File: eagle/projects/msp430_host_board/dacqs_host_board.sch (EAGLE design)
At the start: 31 parts, among them J1 MOL-KK-4P-V, J2 MOL-KK-4P-V, J3 MOL-KK-4P-V, J4 MOL-KK-4P-V, J5 MOL-KK-5P-V, J6 MOL-KK-3P-V, U1 Value, U2 Value, Y1 32.768kHz, Y2 4MHz, Y3 32.768kHz, Y4 4MHz

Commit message: Changes to MSP connections
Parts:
- added J7: MOL-KK-5P-V, daqcs_host:MOLKK_5PIN_5RA_RA
- added J8: MOL-KK-3P-RA, daqcs_host:MOLKK_3PIN_3RA_RA
- added R4, R5, R6, R7: 2.61k, daqcs_host:RES_2R61_0603
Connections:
- removed net SD_CS: U2.P4.0_A8
- removed net SENSE_SCL: U2.P6.5_UCB3SOMI_UCB3SCL
- removed net SENSE_SDA: U2.P6.4_UCB3SIMO_UCB3SDA
- new net SD_SS: U2.P5.7_UCA2STE_TA4.1_MCLK
- new net SENSE_SCL_1: R4.1, U2.P1.7_TB0.4_UCB0SOMI_UCB0SCL_TA1.0
- new net SENSE_SCL_2: R7.1, U2.P5.1_UCB1SOMI_UCB1SCL
- new net SENSE_SDA_1: R5.1, U2.P1.6_TB0.3_UCB0SIMO_UCB0SDA_TA0.0
- new net SENSE_SDA_2: R6.1, U2.P5.0_UCB1SIMO_UCB1SDA
- net +3V3: now also R4.2, R5.2, R6.2, R7.2
- net ACT_CURRENT_IN: now also J8.2
- net ACT_SPEED_IN: now also J8.1
- net COMMS_MISO: now also U1.P5.1_UCB1SOMI_UCB1SCL; no longer U1.P7.1_UCB2SOMI_UCB2SCL
- net COMMS_MOSI: now also U1.P5.0_UCB1SIMO_UCB1SDA; no longer U1.P7.0_UCB2SIMO_UCB2SDA
- net COMMS_SCLK: now also U1.P5.2_UCB1CLK_TA4CLK; no longer U1.P7.2_UCB2CLK
- net COMMS_SS: now also U1.P5.3_UCB1STE; no longer U1.P1.5_TB0.2_UCA0CLK_A5_C5
- net CURRENT_PWM_OUT: now also J7.2, U2.P1.3_TA1.2_UCB0STE_A3_C3; no longer U2.P3.7_TB0.6
- net DIR_MOTOR_OUT: now also J7.4
- net EN_MOTOR_OUT: now also J7.3
- net GND: now also J7.5, J8.3
- net IMU_MISO: now also U2.P2.6_TB0.1_UCA1RXD_UCA1SOMI; no longer U2.P7.1_UCB2SOMI_UCB2SCL
- net IMU_MOSI: now also U2.P2.5_TB0.0_UCA1TXD_UCA1SIMO; no longer U2.P7.0_UCB2SIMO_UCB2SDA
- net IMU_SCLK: now also U2.P2.4_TA1.0_UCA1CLK_A7_C11; no longer U2.P7.2_UCB2CLK
- net IMU_SS: now also U2.P2.3_TA0.0_UCA1STE_A6_C10; no longer U2.P1.5_TB0.2_UCA0CLK_A5_C5
- net MSP_MISO: now also U1.P1.7_TB0.4_UCB0SOMI_UCB0SCL_TA1.0, U2.P2.1_TB0.0_UCA0RXD_UCA0SOMI; no longer U1.P5.1_UCB1SOMI_UCB1SCL, U2.P5.1_UCB1SOMI_UCB1SCL
- net MSP_MOSI: now also U1.P1.6_TB0.3_UCB0SIMO_UCB0SDA_TA0.0, U2.P2.0_TB0.6_UCA0TXD_UCA0SIMO_TB0CLK_ACLK; no longer U1.P5.0_UCB1SIMO_UCB1SDA, U2.P5.0_UCB1SIMO_UCB1SDA
- net MSP_SCLK: now also U1.P2.2_TB0.2_UCB0CLK, U2.P1.5_TB0.2_UCA0CLK_A5_C5; no longer U1.P5.2_UCB1CLK_TA4CLK, U2.P5.2_UCB1CLK_TA4CLK
- net MSP_SS: now also U1.P1.3_TA1.2_UCB0STE_A3_C3; no longer U1.P1.4_TB0.1_UCA0STE_A4_C4
- net SD_MISO: now also U2.P5.5_UCA2RXD_UCA2SOMI_ACLK; no longer U2.P1.7_TB0.4_UCB0SOMI_UCB0SCL_TA1.0
- net SD_MOSI: now also U2.P5.4_UCA2TXD_UCA2SIMO_TB0OUTH; no longer U2.P1.6_TB0.3_UCB0SIMO_UCB0SDA_TA0.0
- net SD_SCLK: now also U2.P5.6_UCA2CLK_TA4.0_SMCLK; no longer U2.P2.2_TB0.2_UCB0CLK
- net SPEED_PWM_OUT: now also J7.1, U2.P1.2_TA1.1_TA0CLK_COUT_A2_C2; no longer U2.P3.6_TB0.5

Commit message: Added sensors, sd card and updated msp pinout for motor control
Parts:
- added C16: 1000pF, daqcs_host:CAP_1000PF0_0603
- added C17, C18, C20: 100nF, daqcs_host:CAP_100NF0_0603
- added C19: 1uF, daqcs_host:CAP_1UF0_0603
- added J10, J9: MOL-KK-3P-V, daqcs_host:MOLKK_3PIN_3V_V
- added J11: CLM-112-02-L-D, SAMTEC-BCS-CES-CLx_By_element14_Batch_1:CLM-112-02-L-D
- added J12: (no value), SparkFun-Connectors:M02PTH
- added R10, R11, R12, R13, R14, R15, R9: 0, daqcs_host:RES_0R0_0603
- added R16, R8: 47k, daqcs_host:RES_47R0_0603
- added R17: 100k, daqcs_host:RES_100R0_0603
- added S2: SWITCH-MOMENTARY-2PTH, daqcs_host:SWITCH-MOMENTARY-2PTH
- added U$1: MICROSD, daqcs_host:MICROSD
- added U3: PCT2075D,118, daqcs_host:PCT2075D,118SOIC8
- added U4: MS560702BA03-50, daqcs_host:MS5607-02BA03_8SMD
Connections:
- new net +5V: J11.10, J11.11, J11.12
- new net IMU_RST: J12.2, U2.P2.7
- new net N$22: R9.2, U3.A0
- new net N$23: R10.2, U3.A1
- new net N$24: R11.2, U3.A2
- new net N$25: R12.1, U3.OS
- new net N$26: R12.2
- new net N$27: R15.2, U4.CSB@1
- new net N$28: R14.2, U4.CSB@2
- new net N$29: R13.1, U4.SDO
- new net N$30: R13.2
- new net N$32: J11.8, J12.1
- new net N$34: R17.2, U$1.CARD_DETECT1
- new net SD_CS: R16.2, U$1.CS, U2.P4.2_A10
- net +3V3: now also C17.1, C18.1, C19.1, C20.1, R16.1, R17.1, R8.2, U$1.VDD, U3.VCC, U4.PS, U4.VDD
- net ACT_CURRENT_IN: now also U2.P3.1_A13_C13; no longer U2.P3.0_A12_C12
- net ACT_SPEED_IN: now also U2.P3.0_A12_C12; no longer U2.P3.1_A13_C13
- net DIR_MOTOR_OUT: now also U2.P4.1_A9; no longer U2.P4.3_A11
- net EN_MOTOR_OUT: now also U2.P4.0_A8; no longer U2.P4.2_A10
- net GND: now also C16.1, C17.2, C18.2, C19.2, C20.2, J10.3, J11.13, J11.14, J11.15, J9.3, R10.1, R11.1, R14.1, R15.1, R9.1, S2.1, U$1.CARD_DETECT, U$1.GND, U$1.GND1, U$1.VSS, U3.GND, U4.GND
- net IMU_MISO: now also J11.4
- net IMU_MOSI: now also J11.5
- net IMU_SCLK: now also J11.3
- net IMU_SS: now also J11.6
- net RST_SBWTDIO_MOTOR: now also C16.2, J10.1, R8.1, S2.2
- net SBWTCK_MOTOR: now also J10.2
- net SD_DETECT: now also U2.P3.2_A14_C14; no longer U2.P4.5
- net SD_MISO: now also U$1.DATA_OUT
- net SD_MOSI: now also U$1.DATA_IN
- net SD_SCLK: now also U$1.SCLK
- net SENSE_SCL_1: now also U3.SCL, U4.SCLK
- net SENSE_SCL_2: now also J9.2
- net SENSE_SDA_1: now also U3.SDA, U4.SDI/SDA
- net SENSE_SDA_2: now also J9.1
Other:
- note added: "IMU Connector Header"
- note added: "Jumper header to disable RST if necessary"
- note added: "Pressure Sensor"
- note added: "SD Card Connector"
- note added: "Temperature Sensor"

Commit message: Added Power Management schematic
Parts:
- added C21: 2.2uF, daqcs_host:CAP_2UF2_0603
- added C22: 4.7uF, daqcs_host:CAP_4UF7_0603
- added C23, C24: 1uF, daqcs_host:CAP_1UF0_0603
- added J13: MOL-KK-2-V, daqcs_host:MOLKK_2PIN2V_2V
- added U5: TPS61240DRVR, daqcs_host:TPS61240DRVR
- added U6: LP5907_DBV_5, daqcs_host:LP5907_DBV_5
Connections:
- new net N$36: C21.1, J13.1, U5.EN, U5.VIN
- net +3V3: now also C24.1, U6.VOUT
- net +5V: now also C22.1, C23.1, U5.FB, U5.VOUT, U6.EN, U6.VIN
- net GND: now also C21.2, C22.2, C23.2, C24.2, J13.2, U5.GND, U6.GND
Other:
- note added: "ADD 1uH INDUCTOR!!!"
- note added: "External I2C Pressure Sensor Header"
- note added: "Motor In Header Connection"
- note added: "Motor Out Header Connection"
- note added: "Power Management Schematic"
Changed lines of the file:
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@@
 <setting verticaltext="up"/>
 </settings>
-<grid distance="0.1" unitdist="inch" unit="inch" style="lines" multiple="1" display="yes" altdistance="0.01" altunitdist="inch" altunit="inch"/>
+<grid distance="0.1" unitdist="inch" unit="inch" style="lines" multiple="1" display="no" altdistance="0.01" altunitdist="inch" altunit="inch"/>
 <layers>
 <layer number="1" name="Top" color="4" fill="1" visible="no" active="no"/>
@@
 <part name="SUPPLY18" library="supply2" deviceset="GND" device=""/>
 <part name="SUPPLY19" library="supply2" deviceset="GND" device=""/>
+<part name="FRAME6" library="frames" deviceset="A3L-LOC" device=""/>
+<part name="J13" library="daqcs_host" deviceset="MOLKK_2PIN" device="_2V" technology="2V" value="MOL-KK-2-V"/>
+<part name="U5" library="daqcs_host" deviceset="TPS61240DRVR" device=""/>
+<part name="U6" library="daqcs_host" deviceset="LP5907_DBV_5" device=""/>
+<part name="SUPPLY20" library="supply2" deviceset="GND" device=""/>
+<part name="C21" library="daqcs_host" deviceset="CAP" device="_0603" technology="_2UF2" value="2.2uF"/>
+<part name="C22" library="daqcs_host" deviceset="CAP" device="_0603" technology="_4UF7" value="4.7uF"/>
+<part name="SUPPLY21" library="supply2" deviceset="GND" device=""/>
+<part name="C23" library="daqcs_host" deviceset="CAP" device="_0603" technology="_1UF0" value="1uF"/>
+<part name="C24" library="daqcs_host" deviceset="CAP" device="_0603" technology="_1UF0" value="1uF"/>
+<part name="SUPPLY22" library="supply2" deviceset="GND" device=""/>
+<part name="SUPPLY23" library="supply2" deviceset="GND" device=""/>
 </parts>
 <sheets>
@@
 <sheet>
 <plain>
-<text x="22.86" y="213.36" size="1.778" layer="91">Header Connector for UART_1</text>
-<text x="101.6" y="213.36" size="1.778" layer="91">Header Connector for UART_2</text>
-<text x="22.86" y="160.02" size="1.778" layer="91">Header Connector for UART_3</text>
-<text x="101.6" y="160.02" size="1.778" layer="91">Header Connector for UART_4</text>
-<text x="20.32" y="99.06" size="1.778" layer="91">Header Connector for COMMS_SPI</text>
-<text x="246.38" y="213.36" size="1.778" layer="91">Reset Pushbutton</text>
-<text x="236.22" y="137.16" size="1.778" layer="91">Header Connector for Spi-Bi-Wire</text>
+<text x="15.24" y="213.36" size="2.54" layer="91">Header Connector for UART_1</text>
+<text x="93.98" y="213.36" size="2.54" layer="91">Header Connector for UART_2</text>
+<text x="15.24" y="160.02" size="2.54" layer="91">Header Connector for UART_3</text>
+<text x="93.98" y="160.02" size="2.54" layer="91">Header Connector for UART_4</text>
+<text x="10.16" y="99.06" size="2.54" layer="91">Header Connector for COMMS_SPI</text>
+<text x="243.84" y="213.36" size="2.54" layer="91">Reset Pushbutton</text>
+<text x="226.06" y="137.16" size="2.54" layer="91">Header Connector for Spi-Bi-Wire</text>
 </plain>
 <instances>
@@
 <sheet>
 <plain>
+<text x="30.48" y="218.44" size="2.54" layer="91">Motor Out Header Connection</text>
+<text x="33.02" y="152.4" size="2.54" layer="91">Motor In Header Connection</text>
+<text x="25.4" y="83.82" size="2.54" layer="91">External I2C Pressure Sensor Header</text>
+<text x="213.36" y="127" size="2.54" layer="91">Header Connector for Spi-Bi-Wire</text>
+<text x="228.6" y="215.9" size="2.54" layer="91">Reset Pushbutton </text>
 </plain>
 <instances>
@@
 <sheet>
 <plain>
-<text x="91.44" y="218.44" size="1.778" layer="91">Temperature Sensor</text>
-<text x="269.24" y="218.44" size="1.778" layer="91">Pressure Sensor</text>
-<text x="93.98" y="104.14" size="1.778" layer="91">IMU Connector Header</text>
+<text x="81.28" y="218.44" size="2.54" layer="91">Temperature Sensor</text>
+<text x="264.16" y="218.44" size="2.54" layer="91">Pressure Sensor</text>
+<text x="83.82" y="104.14" size="2.54" layer="91">IMU Connector Header</text>
 <text x="134.62" y="99.06" size="1.778" layer="91">Jumper header to disable RST if necessary</text>
-<text x="256.54" y="106.68" size="1.778" layer="91">SD Card Connector</text>
+<text x="256.54" y="106.68" size="2.54" layer="91">SD Card Connector</text>
 </plain>
 <instances>
@@
 </segment>
 </net>
+</nets>
+</sheet>
+<sheet>
+<plain>
+<text x="104.14" y="210.82" size="1.778" layer="91">ADD 1uH INDUCTOR!!!</text>
+<text x="147.32" y="236.22" size="6.4516" layer="91">Power Management Schematic</text>
+</plain>
+<instances>
+<instance part="FRAME6" gate="G$1" x="0" y="0"/>
+<instance part="J13" gate="G$1" x="53.34" y="198.12"/>
+<instance part="U5" gate="A" x="139.7" y="195.58"/>
+<instance part="U6" gate="A" x="210.82" y="200.66"/>
+<instance part="SUPPLY20" gate="GND" x="88.9" y="165.1"/>
+<instance part="C21" gate="G$1" x="76.2" y="185.42"/>
+<instance part="C22" gate="G$1" x="175.26" y="190.5"/>
+<instance part="SUPPLY21" gate="GND" x="175.26" y="180.34"/>
+<instance part="C23" gate="G$1" x="190.5" y="190.5"/>
+<instance part="C24" gate="G$1" x="269.24" y="187.96"/>
+<instance part="SUPPLY22" gate="GND" x="190.5" y="180.34"/>
+<instance part="SUPPLY23" gate="GND" x="269.24" y="177.8"/>
+</instances>
+<busses>
+</busses>
+<nets>
+<net name="N$36" class="0">
+<segment>
+<pinref part="J13" gate="G$1" pin="1"/>
+<pinref part="U5" gate="A" pin="VIN"/>
+<wire x1="66.04" y1="200.66" x2="76.2" y2="200.66" width="0.1524" layer="91"/>
+<pinref part="U5" gate="A" pin="EN"/>
+<wire x1="76.2" y1="200.66" x2="109.22" y2="200.66" width="0.1524" layer="91"/>
+<wire x1="109.22" y1="200.66" x2="121.92" y2="200.66" width="0.1524" layer="91"/>
+<wire x1="121.92" y1="193.04" x2="109.22" y2="193.04" width="0.1524" layer="91"/>
+<wire x1="109.22" y1="193.04" x2="109.22" y2="200.66" width="0.1524" layer="91"/>
+<junction x="109.22" y="200.66"/>
+<pinref part="C21" gate="G$1" pin="1"/>
+<wire x1="76.2" y1="190.5" x2="76.2" y2="200.66" width="0.1524" layer="91"/>
+<junction x="76.2" y="200.66"/>
+</segment>
+</net>
+<net name="GND" class="0">
+<segment>
+<pinref part="J13" gate="G$1" pin="2"/>
+<wire x1="66.04" y1="195.58" x2="66.04" y2="170.18" width="0.1524" layer="91"/>
+<pinref part="SUPPLY20" gate="GND" pin="GND"/>
+<wire x1="66.04" y1="170.18" x2="76.2" y2="170.18" width="0.1524" layer="91"/>
+<wire x1="76.2" y1="170.18" x2="88.9" y2="170.18" width="0.1524" layer="91"/>
+<wire x1="88.9" y1="170.18" x2="88.9" y2="167.64" width="0.1524" layer="91"/>
+<pinref part="C21" gate="G$1" pin="2"/>
+<wire x1="76.2" y1="182.88" x2="76.2" y2="170.18" width="0.1524" layer="91"/>
+<junction x="76.2" y="170.18"/>
+<pinref part="U5" gate="A" pin="GND"/>
+<wire x1="121.92" y1="185.42" x2="96.52" y2="185.42" width="0.1524" layer="91"/>
+<wire x1="96.52" y1="185.42" x2="96.52" y2="170.18" width="0.1524" layer="91"/>
+<wire x1="96.52" y1="170.18" x2="88.9" y2="170.18" width="0.1524" layer="91"/>
+<junction x="88.9" y="170.18"/>
+</segment>
+<segment>
+<pinref part="C22" gate="G$1" pin="2"/>
+<pinref part="SUPPLY21" gate="GND" pin="GND"/>
+<wire x1="175.26" y1="187.96" x2="175.26" y2="182.88" width="0.1524" layer="91"/>
+</segment>
+<segment>
+<pinref part="C23" gate="G$1" pin="2"/>
+<pinref part="SUPPLY22" gate="GND" pin="GND"/>
+<wire x1="190.5" y1="187.96" x2="190.5" y2="182.88" width="0.1524" layer="91"/>
+</segment>
+<segment>
+<pinref part="C24" gate="G$1" pin="2"/>
+<pinref part="SUPPLY23" gate="GND" pin="GND"/>
+<wire x1="269.24" y1="185.42" x2="269.24" y2="182.88" width="0.1524" layer="91"/>
+<pinref part="U6" gate="A" pin="GND"/>
+<wire x1="269.24" y1="182.88" x2="269.24" y2="180.34" width="0.1524" layer="91"/>
+<wire x1="251.46" y1="190.5" x2="259.08" y2="190.5" width="0.1524" layer="91"/>
+<wire x1="259.08" y1="190.5" x2="259.08" y2="182.88" width="0.1524" layer="91"/>
+<wire x1="259.08" y1="182.88" x2="269.24" y2="182.88" width="0.1524" layer="91"/>
+<junction x="269.24" y="182.88"/>
+</segment>
+</net>
+<net name="+5V" class="0">
+<segment>
+<pinref part="U5" gate="A" pin="VOUT"/>
+<pinref part="C22" gate="G$1" pin="1"/>
+<wire x1="157.48" y1="200.66" x2="165.1" y2="200.66" width="0.1524" layer="91"/>
+<wire x1="165.1" y1="200.66" x2="175.26" y2="200.66" width="0.1524" layer="91"/>
+<wire x1="175.26" y1="200.66" x2="175.26" y2="195.58" width="0.1524" layer="91"/>
+<pinref part="U5" gate="A" pin="FB"/>
+<wire x1="121.92" y1="195.58" x2="114.3" y2="195.58" width="0.1524" layer="91"/>
+<wire x1="114.3" y1="195.58" x2="114.3" y2="208.28" width="0.1524" layer="91"/>
+<wire x1="114.3" y1="208.28" x2="165.1" y2="208.28" width="0.1524" layer="91"/>
+<wire x1="165.1" y1="208.28" x2="165.1" y2="200.66" width="0.1524" layer="91"/>
+<junction x="165.1" y="200.66"/>
+<label x="167.64" y="200.66" size="1.778" layer="95"/>
+<pinref part="U6" gate="A" pin="EN"/>
+<wire x1="175.26" y1="200.66" x2="190.5" y2="200.66" width="0.1524" layer="91"/>
+<junction x="175.26" y="200.66"/>
+<pinref part="U6" gate="A" pin="VIN"/>
+<wire x1="190.5" y1="200.66" x2="203.2" y2="200.66" width="0.1524" layer="91"/>
+<wire x1="203.2" y1="200.66" x2="210.82" y2="200.66" width="0.1524" layer="91"/>
+<wire x1="210.82" y1="195.58" x2="203.2" y2="195.58" width="0.1524" layer="91"/>
+<wire x1="203.2" y1="195.58" x2="203.2" y2="200.66" width="0.1524" layer="91"/>
+<junction x="203.2" y="200.66"/>
+<pinref part="C23" gate="G$1" pin="1"/>
+<wire x1="190.5" y1="200.66" x2="190.5" y2="195.58" width="0.1524" layer="91"/>
+<junction x="190.5" y="200.66"/>
+</segment>
+</net>
+<net name="+3V3" class="0">
+<segment>
+<pinref part="U6" gate="A" pin="VOUT"/>
+<pinref part="C24" gate="G$1" pin="1"/>
+<wire x1="251.46" y1="195.58" x2="269.24" y2="195.58" width="0.1524" layer="91"/>
+<wire x1="269.24" y1="195.58" x2="269.24" y2="193.04" width="0.1524" layer="91"/>
+<wire x1="269.24" y1="195.58" x2="287.02" y2="195.58" width="0.1524" layer="91"/>
+<junction x="269.24" y="195.58"/>
+<label x="279.4" y="195.58" size="1.778" layer="95"/>
+</segment>
+</net>

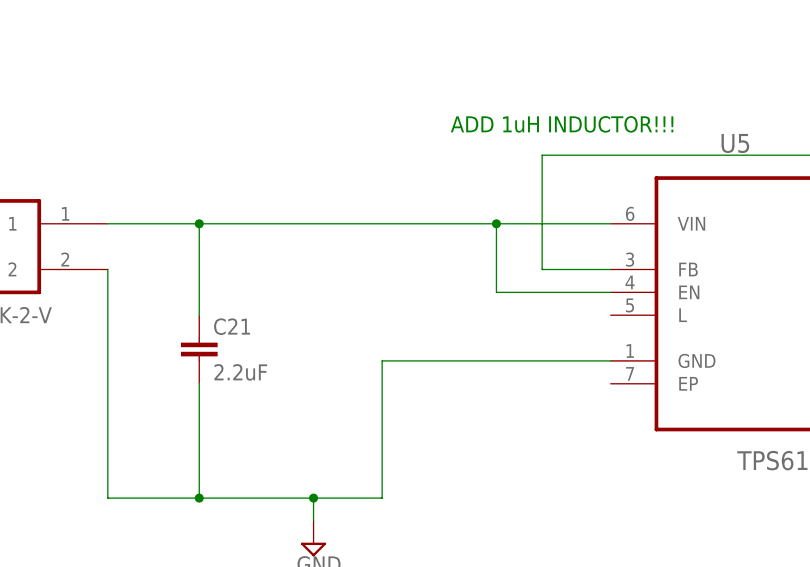
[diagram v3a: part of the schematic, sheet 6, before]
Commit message: Added inductor to power management and added new common library of passive and random parts
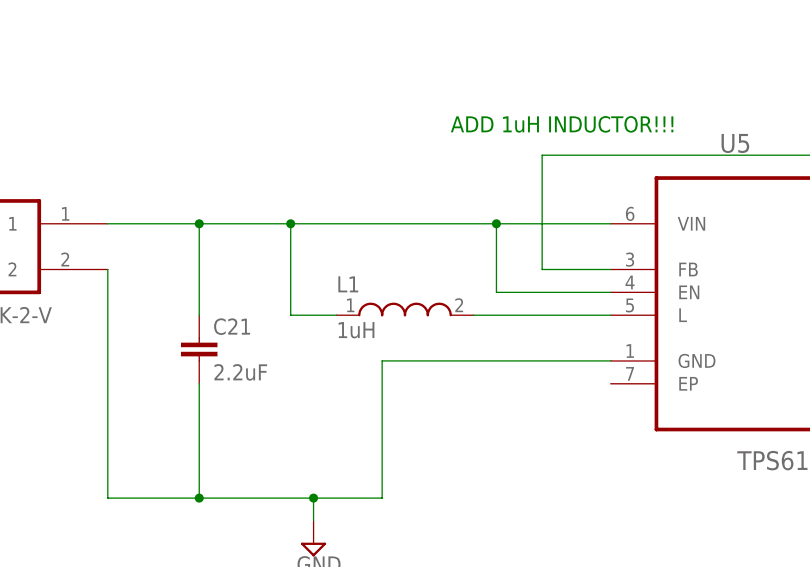
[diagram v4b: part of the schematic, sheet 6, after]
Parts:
- added L1: 1uH, daqcs_host:IND_1UH0_0805
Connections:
- new net N$37: L1.2, U5.L
- net N$36: now also L1.1
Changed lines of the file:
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@@
 <part name="SUPPLY22" library="supply2" deviceset="GND" device=""/>
 <part name="SUPPLY23" library="supply2" deviceset="GND" device=""/>
+<part name="L1" library="daqcs_host" deviceset="IND" device="_0805" technology="_1UH0" value="1uH"/>
 </parts>
 <sheets>
@@
 <instance part="SUPPLY22" gate="GND" x="190.5" y="180.34"/>
 <instance part="SUPPLY23" gate="GND" x="269.24" y="177.8"/>
+<instance part="L1" gate="G$1" x="99.06" y="190.5"/>
 </instances>
 <busses>
@@
 <wire x1="66.04" y1="200.66" x2="76.2" y2="200.66" width="0.1524" layer="91"/>
 <pinref part="U5" gate="A" pin="EN"/>
-<wire x1="76.2" y1="200.66" x2="109.22" y2="200.66" width="0.1524" layer="91"/>
+<wire x1="76.2" y1="200.66" x2="86.36" y2="200.66" width="0.1524" layer="91"/>
+<wire x1="86.36" y1="200.66" x2="109.22" y2="200.66" width="0.1524" layer="91"/>
 <wire x1="109.22" y1="200.66" x2="121.92" y2="200.66" width="0.1524" layer="91"/>
 <wire x1="121.92" y1="193.04" x2="109.22" y2="193.04" width="0.1524" layer="91"/>
@@
 <wire x1="76.2" y1="190.5" x2="76.2" y2="200.66" width="0.1524" layer="91"/>
 <junction x="76.2" y="200.66"/>
+<wire x1="91.44" y1="190.5" x2="86.36" y2="190.5" width="0.1524" layer="91"/>
+<wire x1="86.36" y1="190.5" x2="86.36" y2="200.66" width="0.1524" layer="91"/>
+<junction x="86.36" y="200.66"/>
+<pinref part="L1" gate="G$1" pin="1"/>
 </segment>
 </net>
@@
 </segment>
 </net>
+<net name="N$37" class="0">
+<segment>
+<pinref part="U5" gate="A" pin="L"/>
+<wire x1="106.68" y1="190.5" x2="121.92" y2="190.5" width="0.1524" layer="91"/>
+<pinref part="L1" gate="G$1" pin="2"/>
+</segment>
+</net>
